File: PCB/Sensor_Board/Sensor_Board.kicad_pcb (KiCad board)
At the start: 2 copper layers, 90 x 83 mm, 4 parts, among them J1 Conn_01x08_Socket, J2 Conn_01x06_Socket, J3 Conn_01x04_Socket, J4 Conn_01x07_Socket

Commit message: Added Module
Added Ult. GPS Breakout V3
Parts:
- added J5: Conn_01x09_Socket, Connector_PinSocket_2.54mm:PinSocket_1x09_P2.54mm_Vertical, F.Cu at (118.5, 63.4)
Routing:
- net +3.3V: track 74.0 -> 103.3 mm

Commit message: added connector
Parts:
- added J6: SE2-30, SE2-30:SE2-30, F.Cu at (145.2, 63.8)
- moved J3 84.3 mm to (113.4, 145.6), turned to 90 degrees
- moved J2 66.6 mm to (110.9, 131.0), turned to 90 degrees
- moved J5 54.8 mm to (155.1, 104.2)
- moved J4 53.9 mm to (153.7, 133.5)
- moved J1 51.7 mm to (182.1, 133.5)
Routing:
- net +3.3V: track 103.3 -> 116.0 mm
- net /SDA: track 57.8 -> 50.3 mm
- net /SCL: track 64.6 -> 58.2 mm
- added copper zone on B.Cu, net GND
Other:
- board size 90 x 83 mm -> 90 x 90 mm

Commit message: routed all traces to connector
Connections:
- J6 pad 1: (no net) -> unconnected-(J6-GPIO_14-Pad1)
- J6 pad 10: (no net) -> unconnected-(J6-GPIO_12-Pad10)
- J6 pad 11: (no net) -> unconnected-(J6-GPIO_16-Pad11)
- J6 pad 12: (no net) -> unconnected-(J6-GPIO_20-Pad12)
- J6 pad 13: (no net) -> unconnected-(J6-GPIO_21-Pad13)
- J6 pad 14: (no net) -> unconnected-(J6-NC-Pad14)
- J6 pad 15: (no net) -> unconnected-(J6-NC-Pad15)
- J6 pad 16: (no net) -> unconnected-(J6-NC-Pad16)
- J6 pad 17: (no net) -> unconnected-(J6-NC-Pad17)
- J6 pad 18: (no net) -> unconnected-(J6-NC-Pad18)
- J6 pad 19: (no net) -> unconnected-(J6-NC-Pad19)
- J6 pad 2: (no net) -> unconnected-(J6-GPIO_15-Pad2)
- J6 pad 20: (no net) -> unconnected-(J6-NC-Pad20)
- J6 pad 21: (no net) -> unconnected-(J6-NC-Pad21)
- J6 pad 22: (no net) -> unconnected-(J6-NC-Pad22)
- J6 pad 23: (no net) -> +3.3V
- J6 pad 24: (no net) -> unconnected-(J6-5V-Pad24)
- J6 pad 25: (no net) -> unconnected-(J6-5V-Pad25)
- J6 pad 26: (no net) -> unconnected-(J6-5V-Pad26)
- J6 pad 27: (no net) -> unconnected-(J6-VBus-Pad27)
- J6 pad 28: (no net) -> unconnected-(J6-VBus-Pad28)
- J6 pad 29: (no net) -> GND
- J6 pad 3: (no net) -> unconnected-(J6-GPIO_18-Pad3)
- J6 pad 30: (no net) -> GND
- J6 pad 31: (no net) -> /SDA
- J6 pad 32: (no net) -> /SCL
- J6 pad 33: (no net) -> /RX
- J6 pad 34: (no net) -> unconnected-(J6-GPIO_17-Pad34)
- J6 pad 35: (no net) -> unconnected-(J6-GPIO_27-Pad35)
- J6 pad 36: (no net) -> unconnected-(J6-GPIO_22-Pad36)
- J6 pad 37: (no net) -> unconnected-(J6-GPIO_10-Pad37)
- J6 pad 38: (no net) -> unconnected-(J6-GPIO_9-Pad38)
- J6 pad 39: (no net) -> unconnected-(J6-GPIO_11-Pad39)
- J6 pad 4: (no net) -> unconnected-(J6-GPIO_23-Pad4)
- J6 pad 40: (no net) -> unconnected-(J6-GPIO_0-Pad40)
- J6 pad 41: (no net) -> /TX
- J6 pad 42: (no net) -> unconnected-(J6-GPIO_6-Pad42)
- J6 pad 43: (no net) -> unconnected-(J6-GPIO_13-Pad43)
- J6 pad 44: (no net) -> unconnected-(J6-GPIO_19-Pad44)
- J6 pad 45: (no net) -> unconnected-(J6-GPIO_26-Pad45)
- J6 pad 46: (no net) -> unconnected-(J6-NC-Pad46)
- J6 pad 47: (no net) -> unconnected-(J6-NC-Pad47)
- J6 pad 48: (no net) -> unconnected-(J6-NC-Pad48)
- J6 pad 49: (no net) -> unconnected-(J6-NC-Pad49)
- J6 pad 5: (no net) -> unconnected-(J6-GPIO_24-Pad5)
- J6 pad 50: (no net) -> unconnected-(J6-NC-Pad50)
- J6 pad 51: (no net) -> unconnected-(J6-NC-Pad51)
- J6 pad 52: (no net) -> unconnected-(J6-NC-Pad52)
- J6 pad 53: (no net) -> +3.3V
- J6 pad 54: (no net) -> unconnected-(J6-5V-Pad54)
- J6 pad 55: (no net) -> unconnected-(J6-5V-Pad55)
- J6 pad 56: (no net) -> unconnected-(J6-5V-Pad56)
- J6 pad 57: (no net) -> unconnected-(J6-VBus-Pad57)
- J6 pad 58: (no net) -> unconnected-(J6-VBus-Pad58)
- J6 pad 59: (no net) -> GND
- J6 pad 6: (no net) -> unconnected-(J6-GPIO_25-Pad6)
- J6 pad 60: (no net) -> GND
- J6 pad 7: (no net) -> unconnected-(J6-GPIO_8-Pad7)
- J6 pad 8: (no net) -> unconnected-(J6-GPIO_7-Pad8)
- J6 pad 9: (no net) -> unconnected-(J6-GPIO_1-Pad9)
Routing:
- net +3.3V: track 116.0 -> 167.4 mm, vias 0 -> 1

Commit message: forgot to save
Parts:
- moved J3 16.3 mm to (127.0, 136.5), turned to 180 degrees
- moved J2 8.20 mm to (112.4, 139.1), turned to 180 degrees
- moved J1 2.91 mm to (179.5, 132.1)
- moved J4 2.91 mm to (151.2, 132.1)
- moved J5 2.82 mm to (152.5, 103.0)
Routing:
- net /SDA: track 50.3 -> 124.3 mm
- net /SCL: track 58.2 -> 131.5 mm
- net /RX: track 0.00 -> 68.1 mm
- net /TX: track 0.00 -> 57.2 mm
- net +3.3V: track 167.4 -> 165.1 mm, vias 1 -> 4

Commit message: added keep-out zone for connector, added logo to back
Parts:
- added G***: LOGO, SE2-30:Rocketry_Logo_Symbol, B.Cu at (145.2, 107.6)
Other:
- board text added: "Made by: Manas Moondra Grant Gardner Yen Do Elliott Suh Brandon Mueller Daniel Phan"

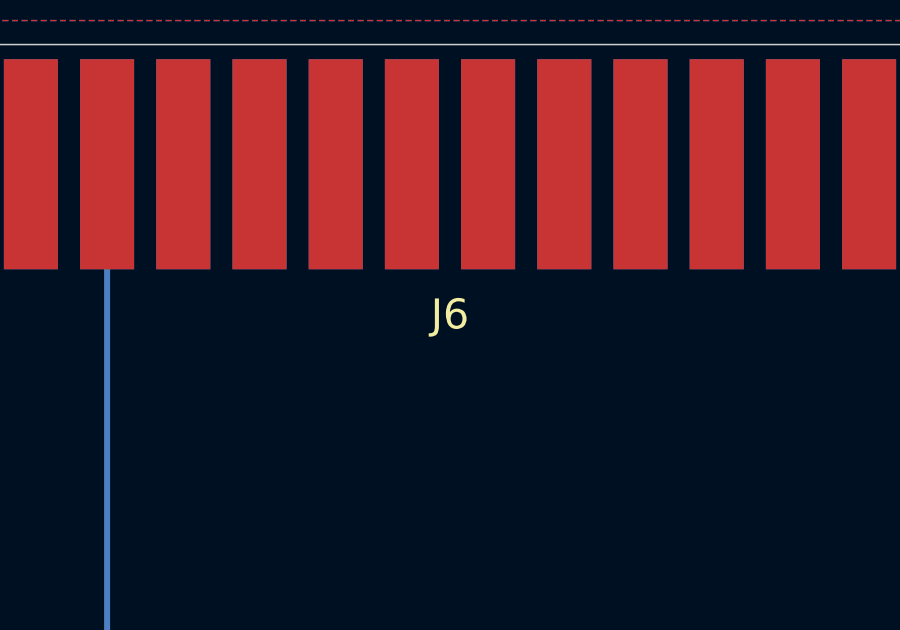
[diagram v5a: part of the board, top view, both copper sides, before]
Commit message: updated footprint from lib
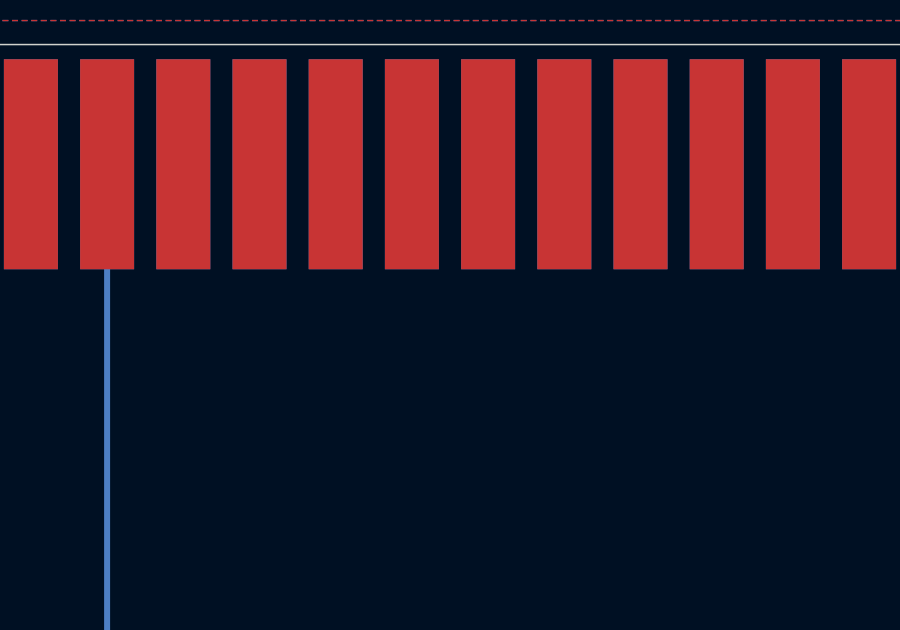
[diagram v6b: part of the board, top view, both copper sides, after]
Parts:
- removed G***: LOGO, SE2-30:Rocketry_Logo_Symbol
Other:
- board text removed: "Made by: Manas Moondra Grant Gardner Yen Do Elliott Suh Brandon Mueller Daniel Phan"

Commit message: small edits
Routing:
- net +3.3V: track 165.1 -> 165.8 mm
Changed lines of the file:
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@@
 	)
 	(segment
-		(start 151.195 132.105)
-		(end 144.235 139.065)
+		(start 164.25 70.950003)
+		(end 164.25 63.79)
 		(width 0.75)
 		(layer "F.Cu")
@@
 	)
 	(segment
-		(start 156.218 103.05)
-		(end 152.5 103.05)
+		(start 151.195 132.105)
+		(end 144.235 139.065)
 		(width 0.75)
 		(layer "F.Cu")
@@
 	)
 	(segment
-		(start 164.25 71)
-		(end 164.25 63.79)
+		(start 164.25 70.950003)
+		(end 164.25 95.018)
 		(width 0.75)
 		(layer "F.Cu")
@@
 	)
 	(segment
-		(start 164.25 95.018)
-		(end 164.25 71)
+		(start 156.218 103.05)
+		(end 152.5 103.05)
 		(width 0.75)
 		(layer "F.Cu")
@@
 		(net 4)
 	)
-	(via blind
-		(at 164.25 71)
+	(via
+		(at 164.25 70.950003)
 		(size 0.6)
 		(drill 0.3)
@@
 		(net 4)
 	)
-	(via blind
-		(at 164.25 70)
+	(via
+		(at 164.25 70.25)
 		(size 0.6)
 		(drill 0.3)
@@
 		(net 4)
 	)
-	(via blind
-		(at 164.25 70.5)
+	(via
+		(at 164.25 71.650006)
 		(size 0.6)
 		(drill 0.3)
@@
 		(net 4)
 	)
-	(via blind
+	(via
 		(at 164.25 69.5)
 		(size 0.6)
@@
 	(segment
 		(start 164.25 63.79)
-		(end 164.25 71)
+		(end 164.25 71.650006)
 		(width 0.75)
 		(layer "B.Cu")
